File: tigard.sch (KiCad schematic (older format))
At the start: 91 parts, among them J1 USB_C_Receptacle_USB2.0, J2 JTAG, J3 UART, J4 SPI, J5 SWD, J6 I2C, Q1 BSH103, SW1 SW_DP4T, SW2 SW_DPDT, U1 AP7365-18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

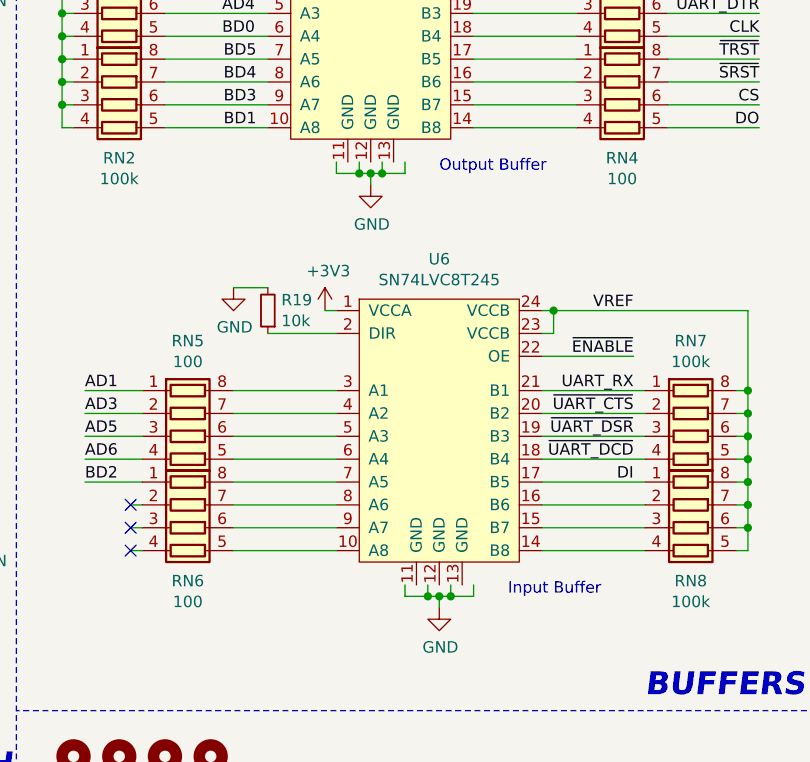
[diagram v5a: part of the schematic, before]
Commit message: Fix buffer symbol (remove PAD)
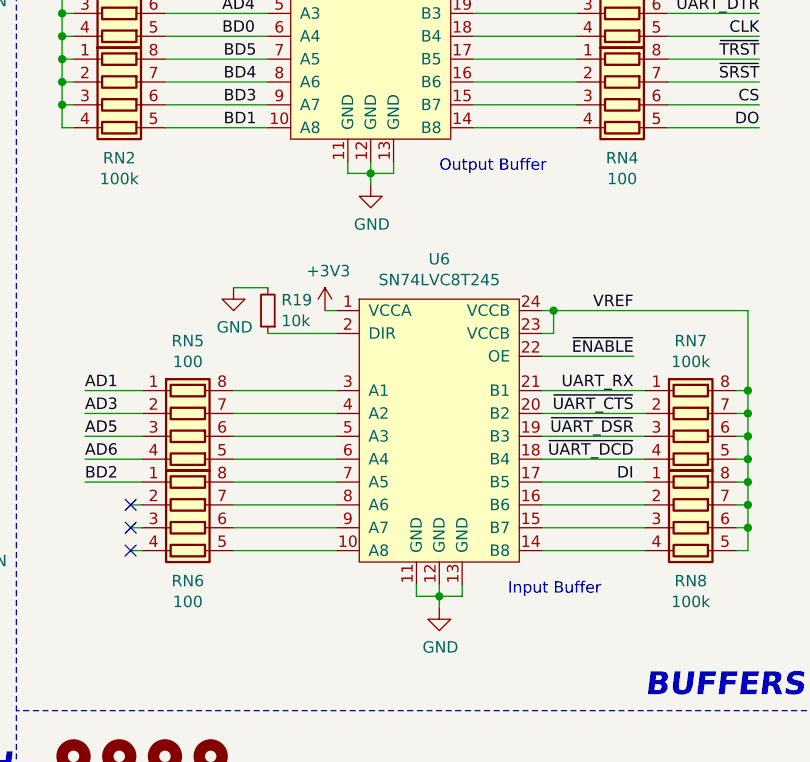
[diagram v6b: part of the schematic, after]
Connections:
- net GND: now also U5.11 (GND), U5.12 (GND), U5.13 (GND), U6.11 (GND), U6.12 (GND), U6.13 (GND)
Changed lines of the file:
@@
 Wire Wire Line
 	6800 6150 7250 6150
-$Comp
-L power:GND #PWR0140
-U 1 1 600BAEA8
-P 6350 6400
-F 0 "#PWR0140" H 6350 6150 50  0001 C CNN
-F 1 "GND" H 6355 6227 50  0000 C CNN
-F 2 "" H 6350 6400 50  0001 C CNN
-F 3 "" H 6350 6400 50  0001 C CNN
-	1    6350 6400
-	1    0    0    -1
-$EndComp
 Text Notes 6650 6350 0    50   ~ 0
 Output Buffer
@@
 	-1   0    0    -1
 $EndComp
-Wire Wire Line
-	6200 6300 6200 6350
-Wire Wire Line
-	6200 6350 6300 6350
-Wire Wire Line
-	6350 6350 6350 6400
-Wire Wire Line
-	6300 6300 6300 6350
-Connection ~ 6300 6350
-Wire Wire Line
-	6300 6350 6350 6350
-Wire Wire Line
-	6400 6300 6400 6350
-Wire Wire Line
-	6400 6350 6350 6350
-Connection ~ 6350 6350
-Wire Wire Line
-	6500 6300 6500 6350
-Wire Wire Line
-	6500 6350 6400 6350
-Connection ~ 6400 6350
-$Comp
-L power:GND #PWR0115
-U 1 1 5F64E0B7
-P 6650 8250
-F 0 "#PWR0115" H 6650 8000 50  0001 C CNN
-F 1 "GND" H 6655 8077 50  0000 C CNN
-F 2 "" H 6650 8250 50  0001 C CNN
-F 3 "" H 6650 8250 50  0001 C CNN
-	1    6650 8250
-	1    0    0    -1
-$EndComp
-Wire Wire Line
-	6500 8150 6500 8200
-Wire Wire Line
-	6500 8200 6600 8200
-Wire Wire Line
-	6650 8200 6650 8250
-Wire Wire Line
-	6600 8150 6600 8200
-Connection ~ 6600 8200
-Wire Wire Line
-	6600 8200 6650 8200
-Wire Wire Line
-	6700 8150 6700 8200
-Wire Wire Line
-	6700 8200 6650 8200
-Connection ~ 6650 8200
-Wire Wire Line
-	6800 8150 6800 8200
-Wire Wire Line
-	6800 8200 6700 8200
-Connection ~ 6700 8200
 NoConn ~ 3700 2400
 NoConn ~ 3700 2500
@@
 Wire Wire Line
 	2600 2650 2600 2700
+$Comp
+L power:GND #PWR?
+U 1 1 60537E1A
+P 6650 8250
+F 0 "#PWR?" H 6650 8000 50  0001 C CNN
+F 1 "GND" H 6655 8077 50  0000 C CNN
+F 2 "" H 6650 8250 50  0001 C CNN
+F 3 "" H 6650 8250 50  0001 C CNN
+	1    6650 8250
+	1    0    0    -1
+$EndComp
+$Comp
+L power:GND #PWR?
+U 1 1 60538E37
+P 6350 6400
+F 0 "#PWR?" H 6350 6150 50  0001 C CNN
+F 1 "GND" H 6355 6227 50  0000 C CNN
+F 2 "" H 6350 6400 50  0001 C CNN
+F 3 "" H 6350 6400 50  0001 C CNN
+	1    6350 6400
+	1    0    0    -1
+$EndComp
+Wire Wire Line
+	6250 6300 6250 6350
+Wire Wire Line
+	6250 6350 6350 6350
+Wire Wire Line
+	6350 6300 6350 6350
+Connection ~ 6350 6350
+Wire Wire Line
+	6450 6300 6450 6350
+Wire Wire Line
+	6450 6350 6350 6350
+Wire Wire Line
+	6350 6400 6350 6350
+Wire Wire Line
+	6550 8150 6550 8200
+Wire Wire Line
+	6550 8200 6650 8200
+Wire Wire Line
+	6650 8200 6650 8250
+Wire Wire Line
+	6650 8150 6650 8200
+Connection ~ 6650 8200
+Wire Wire Line
+	6750 8150 6750 8200
+Wire Wire Line
+	6750 8200 6650 8200
 $EndSCHEMATC

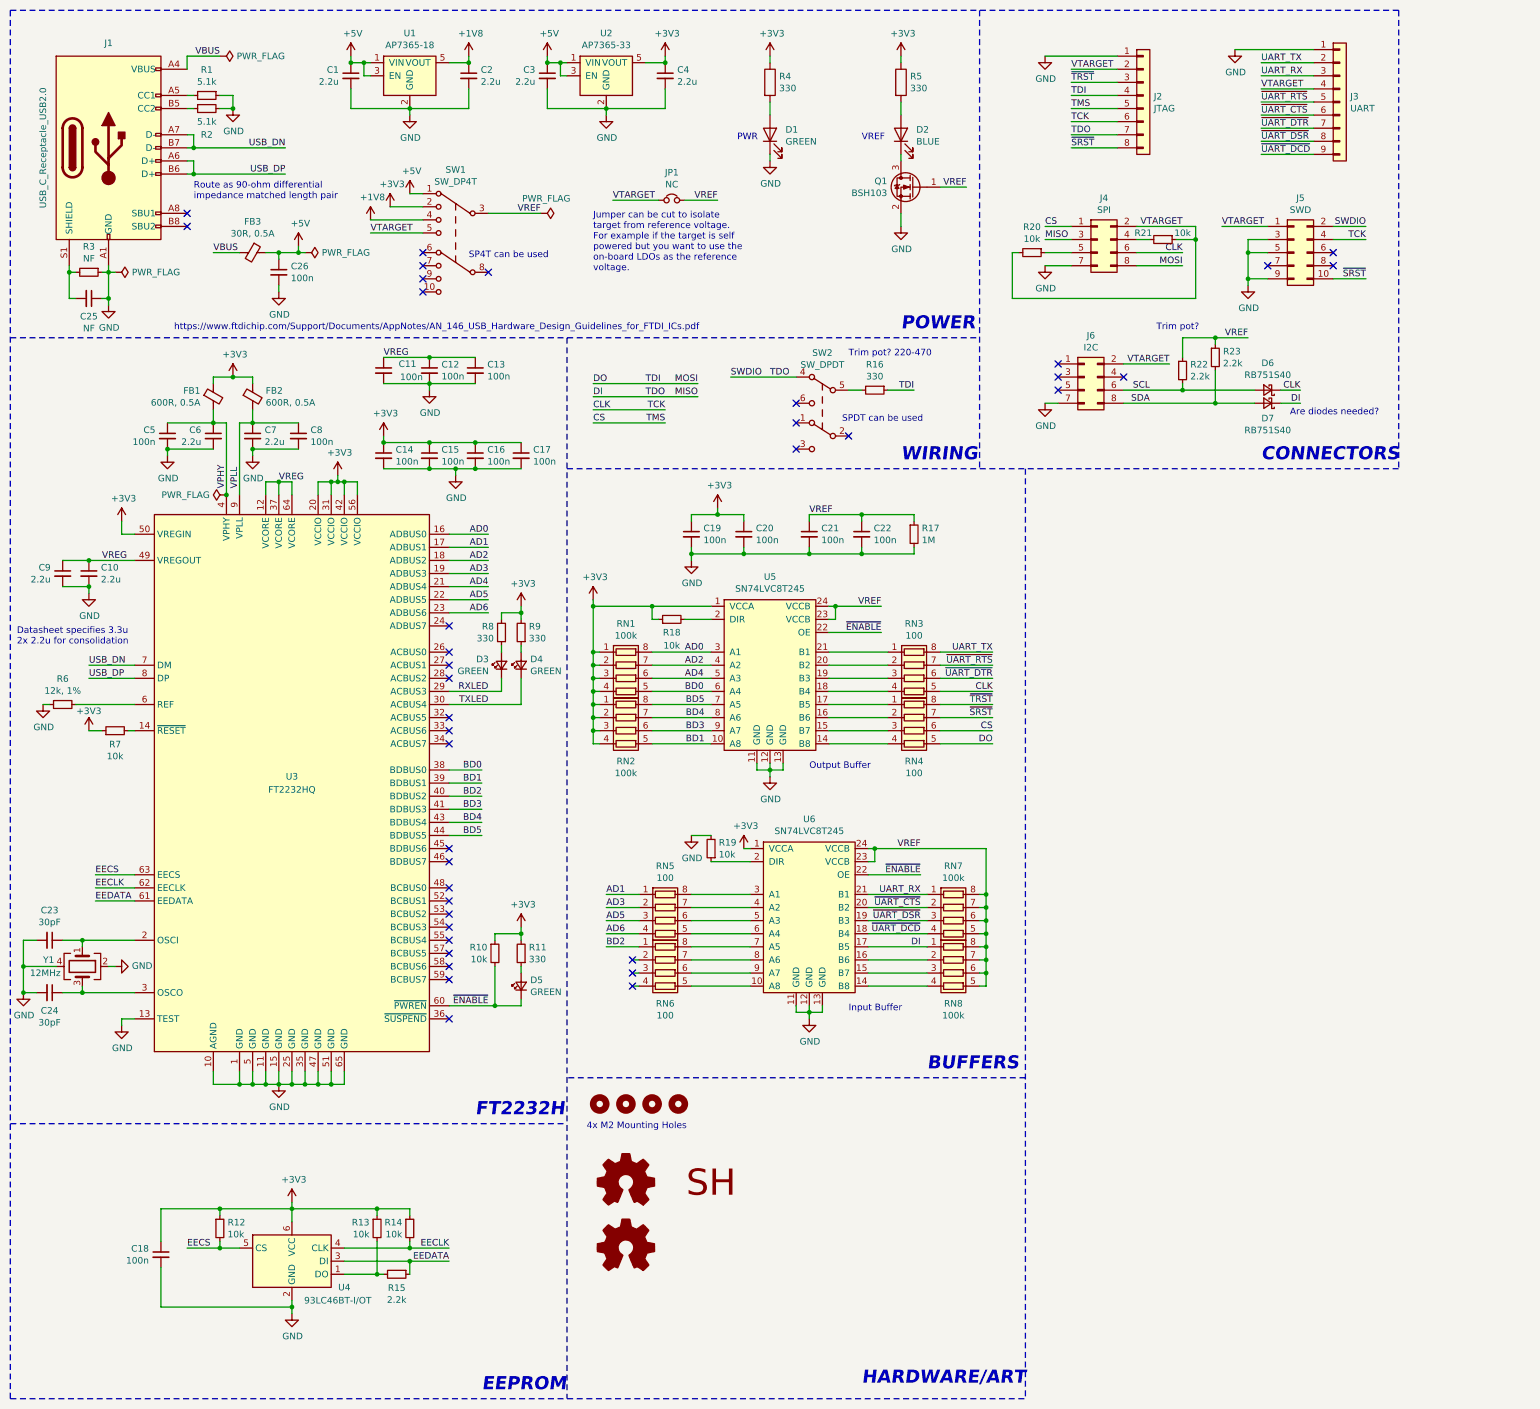
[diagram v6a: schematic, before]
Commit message: Fiddle with labels, add thermal reliefs, add 3D
* VT -> TARGET on switch
* Thermal reliefs for everything but thermal pad vias
* USB C CAD model
* FTDI CAD model
* Align SWD connector
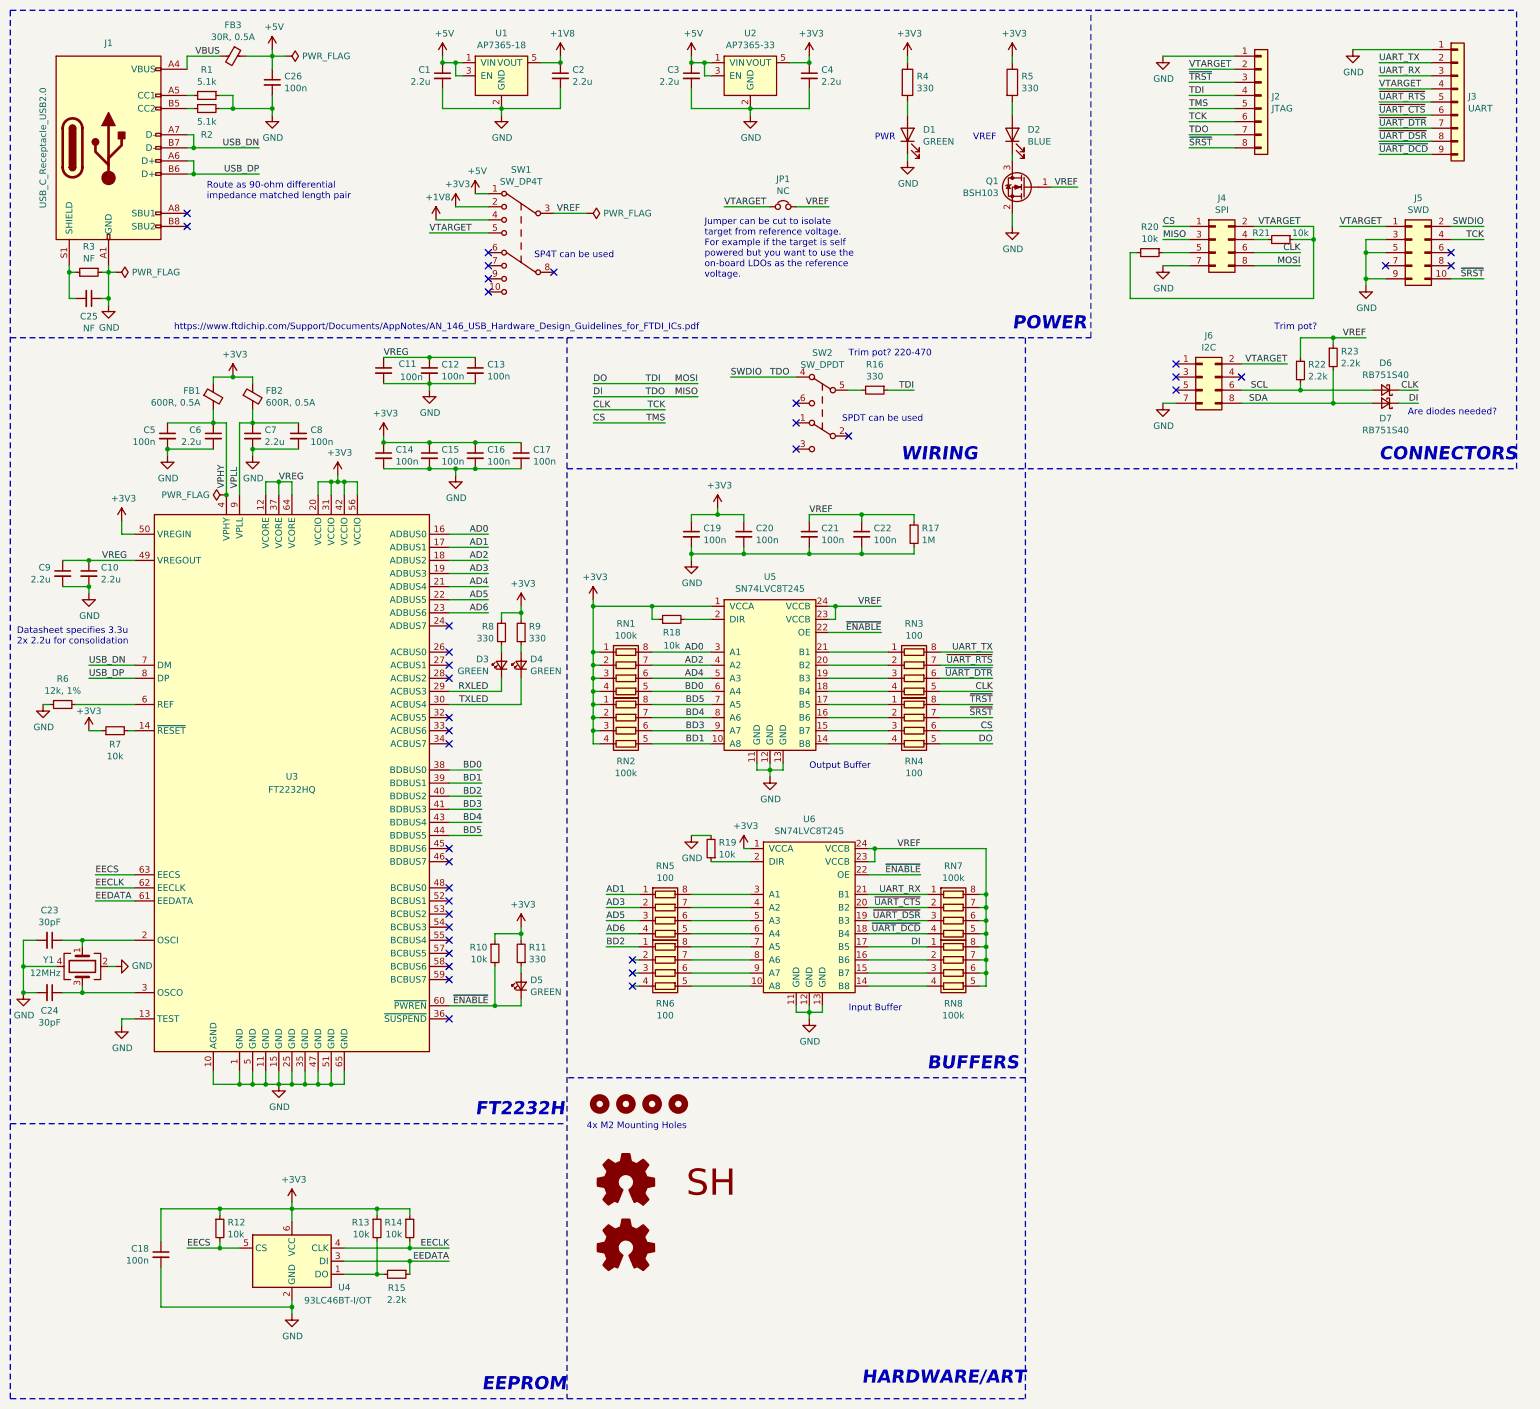
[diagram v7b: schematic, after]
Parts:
- J1: footprint Connector_USB:USB_C_Receptacle_HRO_TYPE-C-31-M-12 -> tigard:USB_C_Receptacle_HRO_TYPE-C-31-M-12
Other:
- moved on the sheet: C1, C2, C26, C3, C4, D1, D2, D6, D7, FB3, J2, J3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

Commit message: Obvious pinheader pin1 markings
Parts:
- J2: footprint Connector_PinHeader_2.54mm:PinHeader_1x08_P2.54mm_Vertical -> tigard:PinHeader_1x08_P2.54mm_Vertical
- J3: footprint Connector_PinHeader_2.54mm:PinHeader_1x09_P2.54mm_Vertical -> tigard:PinHeader_1x09_P2.54mm_Vertical
- J4, J6: footprint Connector_PinHeader_2.54mm:PinHeader_2x04_P2.54mm_Vertical -> tigard:PinHeader_2x04_P2.54mm_Vertical
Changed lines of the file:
@@
 F 0 "J4" H 9800 2617 50  0000 C CNN
 F 1 "SPI" H 9800 2526 50  0000 C CNN
-F 2 "Connector_PinHeader_2.54mm:PinHeader_2x04_P2.54mm_Vertical" H 9750 2300 50  0001 C CNN
+F 2 "tigard:PinHeader_2x04_P2.54mm_Vertical" H 9750 2300 50  0001 C CNN
 F 3 "~" H 9750 2300 50  0001 C CNN
 F 4 "MTP125-1204S1" H 9750 2300 50  0001 C CNN "P/N"
@@
 F 0 "J3" H 11680 1292 50  0000 L CNN
 F 1 "UART" H 11680 1201 50  0000 L CNN
-F 2 "Connector_PinHeader_2.54mm:PinHeader_1x09_P2.54mm_Vertical" H 11600 1250 50  0001 C CNN
+F 2 "tigard:PinHeader_1x09_P2.54mm_Vertical" H 11600 1250 50  0001 C CNN
 F 3 "~" H 11600 1250 50  0001 C CNN
 F 4 "MTP125-1108S1" H 11600 1250 50  0001 C CNN "P/N"
@@
 F 0 "J6" H 9700 3667 50  0000 C CNN
 F 1 "I2C" H 9700 3576 50  0000 C CNN
-F 2 "Connector_PinHeader_2.54mm:PinHeader_2x04_P2.54mm_Vertical" H 9650 3350 50  0001 C CNN
+F 2 "tigard:PinHeader_2x04_P2.54mm_Vertical" H 9650 3350 50  0001 C CNN
 F 3 "~" H 9650 3350 50  0001 C CNN
 F 4 "MTP125-1204S1" H 9650 3350 50  0001 C CNN "P/N"
@@
 F 0 "J2" H 10180 1192 50  0000 L CNN
 F 1 "JTAG" H 10180 1101 50  0000 L CNN
-F 2 "Connector_PinHeader_2.54mm:PinHeader_1x08_P2.54mm_Vertical" H 10100 1200 50  0001 C CNN
+F 2 "tigard:PinHeader_1x08_P2.54mm_Vertical" H 10100 1200 50  0001 C CNN
 F 3 "~" H 10100 1200 50  0001 C CNN
 F 4 "MTP125-1108S1" H 10100 1200 50  0001 C CNN "P/N"
